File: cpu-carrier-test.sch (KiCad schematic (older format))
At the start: 10 parts, among them SW1 SW_Push

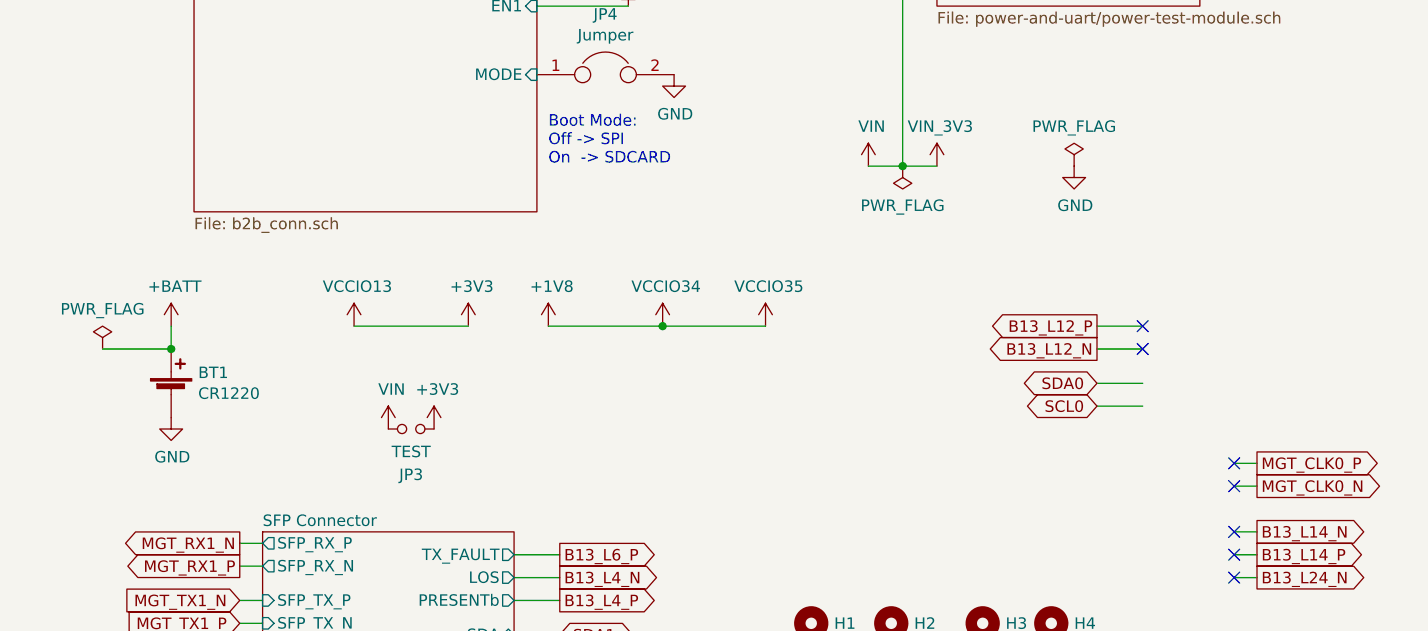
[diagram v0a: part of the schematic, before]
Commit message: connected lan9254 power to board power
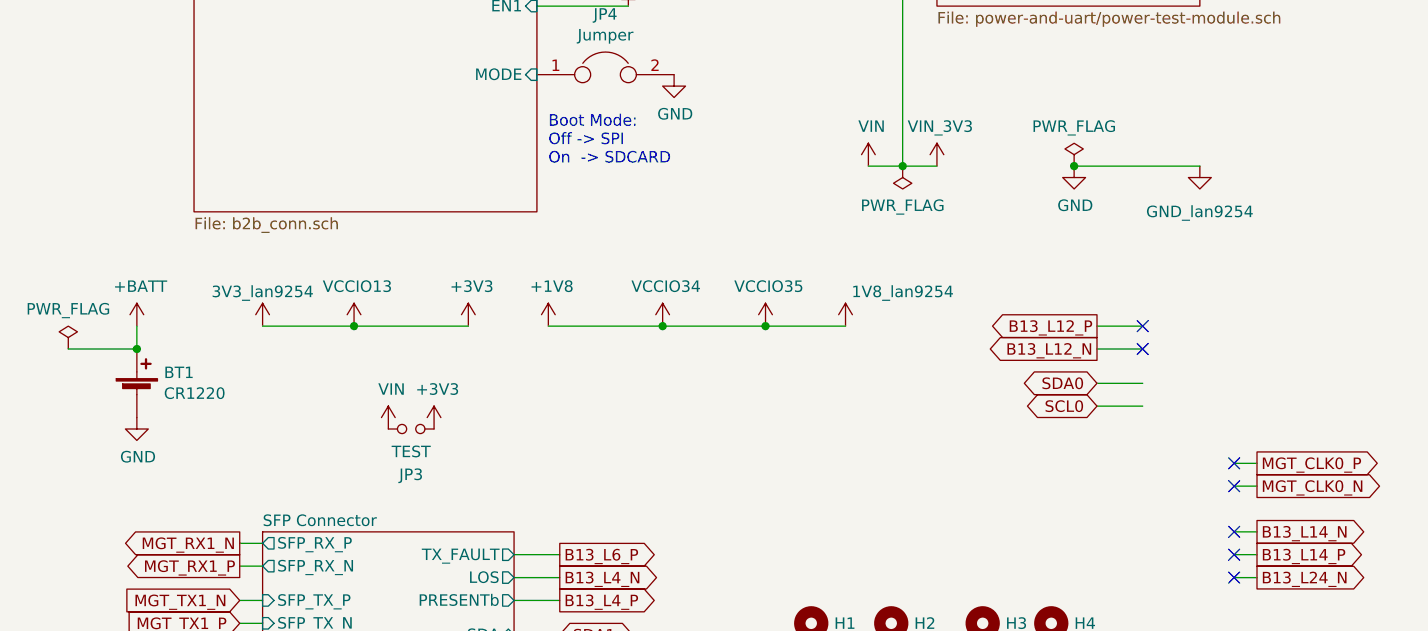
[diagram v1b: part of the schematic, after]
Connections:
- wire segments 84 -> 87
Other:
- moved on the sheet: BT1
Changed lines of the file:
@@
 L Device:Battery_Cell BT?
 U 1 1 5C5255D6
-P 1250 3550
+P 1100 3550
 AR Path="/5CEAC2F1/5C5255D6" Ref="BT?"  Part="1"
 AR Path="/5C5255D6" Ref="BT1"  Part="1"
-F 0 "BT1" H 1368 3646 50  0000 L CNN
-F 1 "CR1220" H 1368 3555 50  0000 L CNN
-F 2 "Battery:BatteryHolder_Keystone_500" V 1250 3610 50  0001 C CNN
-F 3 "~" V 1250 3610 50  0001 C CNN
-F 4 "Keystone" H 1250 3550 50  0001 C CNN "Manufacturer"
-F 5 "500" H 1250 3550 50  0001 C CNN "Part"
-	1    1250 3550
+F 0 "BT1" H 1218 3646 50  0000 L CNN
+F 1 "CR1220" H 1218 3555 50  0000 L CNN
+F 2 "Battery:BatteryHolder_Keystone_500" V 1100 3610 50  0001 C CNN
+F 3 "~" V 1100 3610 50  0001 C CNN
+F 4 "Keystone" H 1100 3550 50  0001 C CNN "Manufacturer"
+F 5 "500" H 1100 3550 50  0001 C CNN "Part"
+	1    1100 3550
 	1    0    0    -1
 $EndComp
@@
 L power:GND #PWR?
 U 1 1 5C5255DD
-P 1250 3650
+P 1100 3650
 AR Path="/5CEAC2F1/5C5255DD" Ref="#PWR?"  Part="1"
 AR Path="/5C5255DD" Ref="#PWR?"  Part="1"
-F 0 "#PWR?" H 1250 3400 50  0001 C CNN
-F 1 "GND" H 1255 3477 50  0000 C CNN
-F 2 "" H 1250 3650 50  0001 C CNN
-F 3 "" H 1250 3650 50  0001 C CNN
-	1    1250 3650
+F 0 "#PWR?" H 1100 3400 50  0001 C CNN
+F 1 "GND" H 1105 3477 50  0000 C CNN
+F 2 "" H 1100 3650 50  0001 C CNN
+F 3 "" H 1100 3650 50  0001 C CNN
+	1    1100 3650
 	1    0    0    -1
 $EndComp
@@
 L power:PWR_FLAG #FLG?
 U 1 1 5C5255E3
-P 950 3350
+P 800 3350
 AR Path="/5CEAC2F1/5C5255E3" Ref="#FLG?"  Part="1"
 AR Path="/5C5255E3" Ref="#FLG?"  Part="1"
-F 0 "#FLG?" H 950 3425 50  0001 C CNN
-F 1 "PWR_FLAG" H 950 3524 50  0000 C CNN
-F 2 "" H 950 3350 50  0001 C CNN
-F 3 "~" H 950 3350 50  0001 C CNN
-	1    950  3350
-	1    0    0    -1
-$EndComp
-Wire Wire Line
-	950  3350 1250 3350
+F 0 "#FLG?" H 800 3425 50  0001 C CNN
+F 1 "PWR_FLAG" H 800 3524 50  0000 C CNN
+F 2 "" H 800 3350 50  0001 C CNN
+F 3 "~" H 800 3350 50  0001 C CNN
+	1    800  3350
+	1    0    0    -1
+$EndComp
+Wire Wire Line
+	800  3350 1100 3350
 $Comp
 L power:+BATT #PWR?
 U 1 1 5C5255EA
-P 1250 3250
+P 1100 3250
 AR Path="/5CEAC2F1/5C5255EA" Ref="#PWR?"  Part="1"
 AR Path="/5C5255EA" Ref="#PWR?"  Part="1"
-F 0 "#PWR?" H 1250 3100 50  0001 C CNN
-F 1 "+BATT" H 1265 3423 50  0000 C CNN
-F 2 "" H 1250 3250 50  0001 C CNN
-F 3 "" H 1250 3250 50  0001 C CNN
-	1    1250 3250
-	1    0    0    -1
-$EndComp
-Wire Wire Line
-	1250 3250 1250 3350
-Connection ~ 1250 3350
+F 0 "#PWR?" H 1100 3100 50  0001 C CNN
+F 1 "+BATT" H 1115 3423 50  0000 C CNN
+F 2 "" H 1100 3250 50  0001 C CNN
+F 3 "" H 1100 3250 50  0001 C CNN
+	1    1100 3250
+	1    0    0    -1
+$EndComp
+Wire Wire Line
+	1100 3250 1100 3350
+Connection ~ 1100 3350
 $Comp
 L trigbox:VCCIO13 #PWR?
@@
 F52 "FPGA_IO1_DIR" I L 8300 6400 50
 $EndSheet
+$Comp
+L lan9254_project:+1V8 #PWR?
+U 1 1 60E7C109
+P 4200 3250
+AR Path="/60DC28BD/60E7C109" Ref="#PWR?"  Part="1"
+AR Path="/60E7C109" Ref="#PWR?"  Part="1"
+AR Path="/60DB2574/60E7C109" Ref="#PWR?"  Part="1"
+AR Path="/60E70F2C/60E7C109" Ref="#PWR?"  Part="1"
+F 0 "#PWR?" H 4200 3100 50  0001 C CNN
+F 1 "+1V8" H 4215 3423 50  0001 C CNN
+F 2 "" H 4200 3250 50  0001 C CNN
+F 3 "" H 4200 3250 50  0001 C CNN
+F 4 "1V8_lan9254" H 4450 3400 50  0000 C CNN "Field4"
+	1    4200 3250
+	1    0    0    -1
+$EndComp
+Wire Wire Line
+	4200 3250 3850 3250
+Connection ~ 3850 3250
+$Comp
+L lan9254_project:+3V3 #PWR?
+U 1 1 60E83E35
+P 1650 3250
+AR Path="/60DC28BD/60E83E35" Ref="#PWR?"  Part="1"
+AR Path="/60E83E35" Ref="#PWR?"  Part="1"
+AR Path="/60DB2574/60E83E35" Ref="#PWR?"  Part="1"
+AR Path="/60E70F2C/60E83E35" Ref="#PWR?"  Part="1"
+F 0 "#PWR?" H 1650 3100 50  0001 C CNN
+F 1 "+3V3" H 1665 3423 50  0001 C CNN
+F 2 "" H 1650 3250 50  0001 C CNN
+F 3 "" H 1650 3250 50  0001 C CNN
+F 4 "3V3_lan9254" H 1650 3400 50  0000 C CNN "Field4"
+	1    1650 3250
+	1    0    0    -1
+$EndComp
+Wire Wire Line
+	1650 3250 2050 3250
+Connection ~ 2050 3250
+$Comp
+L lan9254_project:GND #PWR?
+U 1 1 60E8D23A
+P 5750 2550
+AR Path="/60DC28BD/60E8D23A" Ref="#PWR?"  Part="1"
+AR Path="/60E8D23A" Ref="#PWR?"  Part="1"
+AR Path="/60DB2574/60E8D23A" Ref="#PWR?"  Part="1"
+AR Path="/60E70F2C/60E8D23A" Ref="#PWR?"  Part="1"
+F 0 "#PWR?" H 5750 2300 50  0001 C CNN
+F 1 "GND" H 5755 2377 50  0001 C CNN
+F 2 "" H 5750 2550 50  0001 C CNN
+F 3 "" H 5750 2550 50  0001 C CNN
+F 4 "GND_lan9254" H 5750 2350 50  0000 C CNN "Field4"
+	1    5750 2550
+	1    0    0    -1
+$EndComp
+Wire Wire Line
+	5750 2550 5200 2550
+Connection ~ 5200 2550
 $EndSCHEMATC

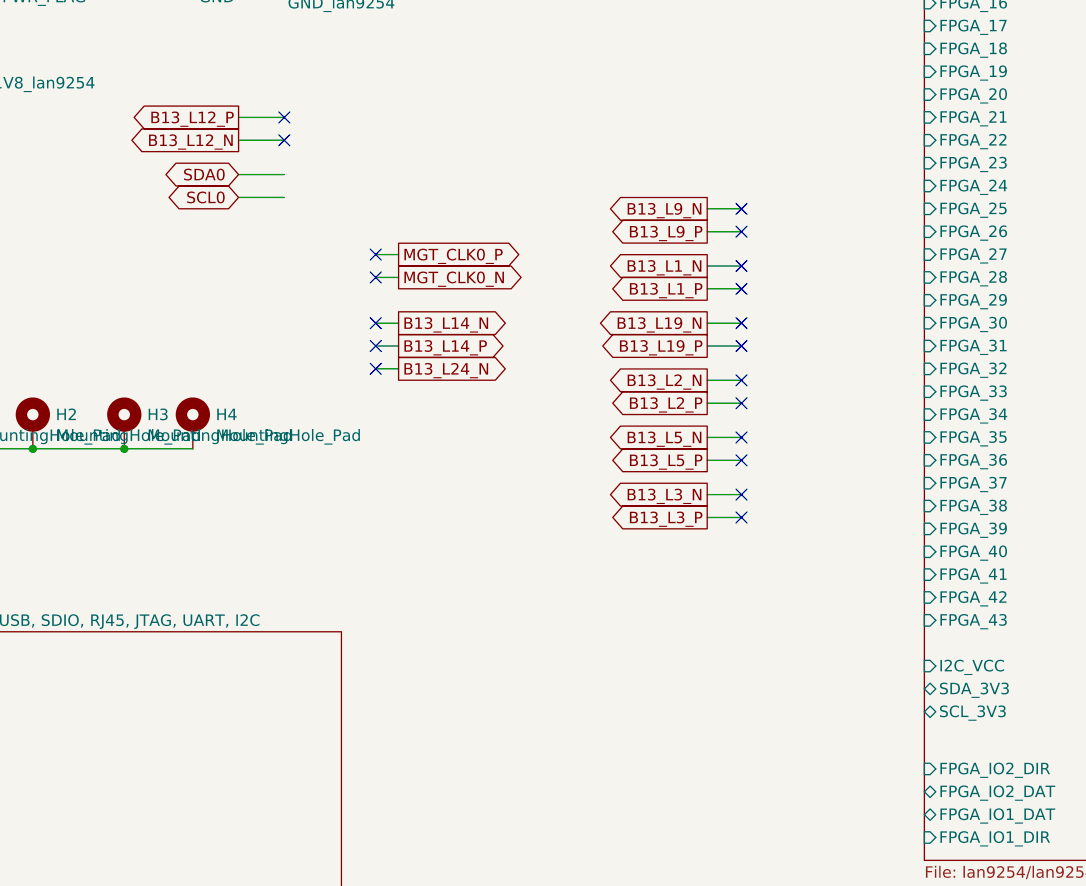
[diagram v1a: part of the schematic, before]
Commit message: connected lan9254 i2c to baseboard SDA0/SDC0
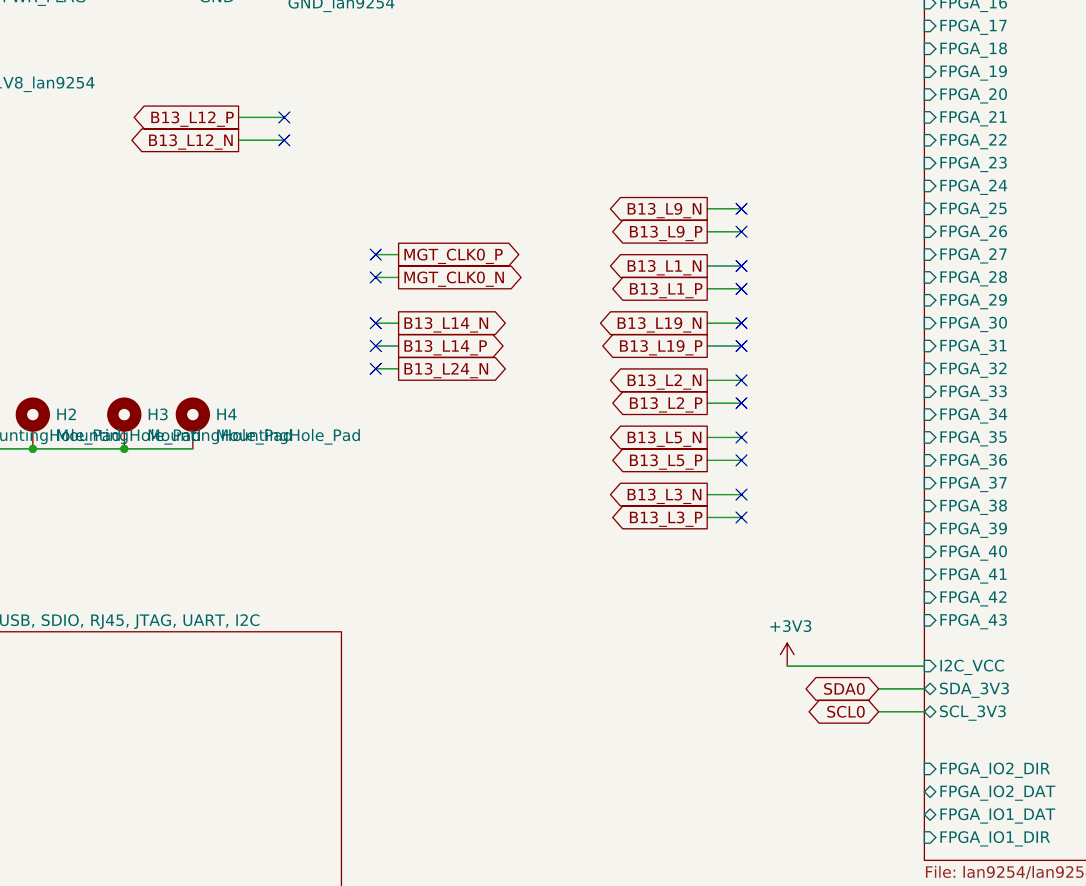
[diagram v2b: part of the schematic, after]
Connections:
- wire segments 87 -> 88
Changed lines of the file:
@@
 $EndSheet
 Wire Wire Line
-	5300 3500 5500 3500
-Wire Wire Line
-	5300 3600 5500 3600
+	8100 5750 8300 5750
+Wire Wire Line
+	8100 5850 8300 5850
 $Sheet
 S 1650 4150 1100 650
@@
 Text GLabel 2950 4700 2    50   BiDi ~ 0
 SCL1
-Text GLabel 5300 3500 0    50   BiDi ~ 0
+Text GLabel 8100 5750 0    50   BiDi ~ 0
 SDA0
-Text GLabel 5300 3600 0    50   BiDi ~ 0
+Text GLabel 8100 5850 0    50   BiDi ~ 0
 SCL0
 $Comp
@@
 	5750 2550 5200 2550
 Connection ~ 5200 2550
+$Comp
+L power:+3V3 #PWR?
+U 1 1 60E53427
+P 7700 5650
+AR Path="/5BE73D36/60E53427" Ref="#PWR?"  Part="1"
+AR Path="/5CEAC2F1/60E53427" Ref="#PWR?"  Part="1"
+AR Path="/60E53427" Ref="#PWR?"  Part="1"
+F 0 "#PWR?" H 7700 5500 50  0001 C CNN
+F 1 "+3V3" H 7715 5823 50  0000 C CNN
+F 2 "" H 7700 5650 50  0001 C CNN
+F 3 "" H 7700 5650 50  0001 C CNN
+	1    7700 5650
+	1    0    0    -1
+$EndComp
+Wire Wire Line
+	7700 5650 8300 5650
 $EndSCHEMATC

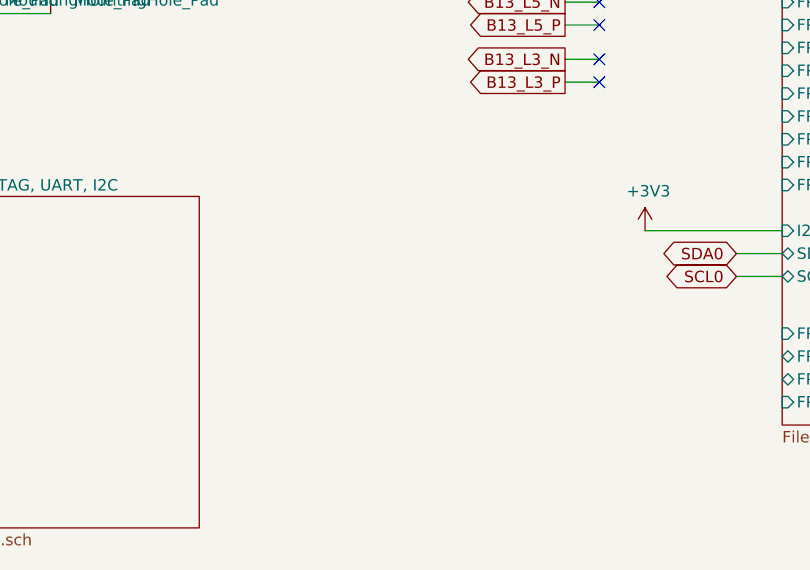
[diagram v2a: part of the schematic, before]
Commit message: converted local- to global labels for B34/B34 B2B pins
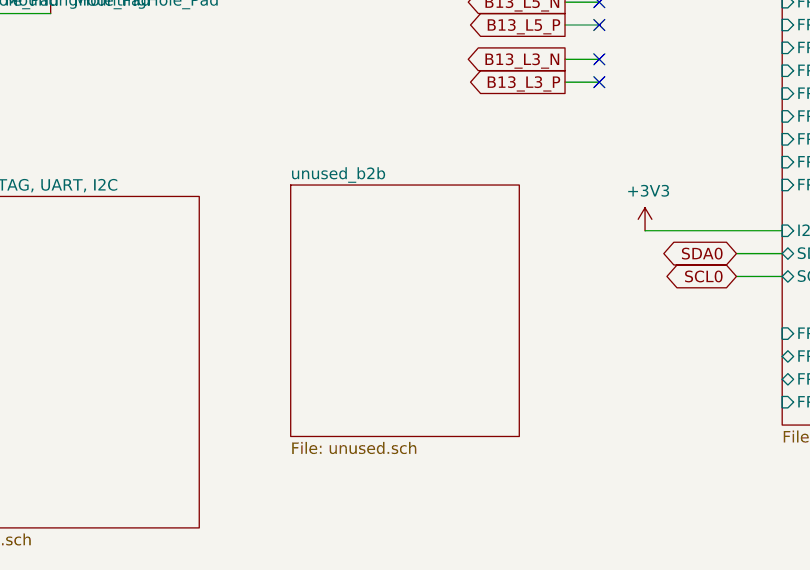
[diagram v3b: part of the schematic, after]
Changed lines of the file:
@@
 $Descr USLetter 11000 8500
 encoding utf-8
-Sheet 1 11
+Sheet 1 12
 Title ""
 Date ""
@@
 Wire Wire Line
 	7700 5650 8300 5650
+$Sheet
+S 6150 5450 1000 1100
+U 60F0717C
+F0 "unused_b2b" 50
+F1 "unused.sch" 50
+$EndSheet
 $EndSCHEMATC

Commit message: cont. work; all connections done now
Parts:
- added D1, D2, D3, D4, D5, D6, D7, D8: LED, LED_SMD:LED_0603_1608Metric, symbol Device:LED
- added R10, R3, R4, R5, R6, R7, R8, R9: 1k, Resistor_SMD:R_0603_1608Metric, symbol Device:R_Small
- R1: renamed from R19; value R10k -> 10k
- R2: renamed from R20; value R10k -> 10k
- renumbered JP3 to JP1, JP4 to JP2
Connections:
- net labels added: B13_L18_N, B13_L18_P, B13_L21_N, B13_L21_P, B34_L12_P, B34_L15_N, B34_L15_P, B34_L18_N, B34_L2_N, B34_L2_P, B34_L6_N, B34_L6_P, B34_L7_N, B34_L8_P, B35_L0, B35_L10_N, B35_L10_P, B35_L11_N, B35_L12_N, B35_L12_P, B35_L13_N, B35_L13_P, B35_L14_N, B35_L14_P, B35_L15_N, B35_L15_P, B35_L16_N, B35_L16_P, B35_L17_N, B35_L17_P, B35_L18_N, B35_L18_P, B35_L20_N, B35_L20_P, B35_L21_P, B35_L22_N, B35_L22_P, B35_L23_N, B35_L23_P, B35_L24_N, B35_L24_P, B35_L25, B35_L2_N, B35_L2_P, B35_L3_N, B35_L4_P, B35_L5_N, B35_L6_N, B35_L7_N, B35_L8_P, B35_L9_N, B35_L9_P
- net labels removed: B13_L11_N, B13_L11_P, B13_L12_N, B13_L12_P, B13_L13_N, B13_L13_P, B13_L14_N, B13_L14_P, B13_L16_N, B13_L16_P, B13_L17_N, B13_L17_P, B13_L19_N, B13_L19_P, B13_L1_N, B13_L1_P, B13_L24_N, B13_L2_N, B13_L2_P, B13_L3_N, B13_L3_P, B13_L5_N, B13_L5_P, B13_L9_N, B13_L9_P, MGT_CLK0_N, MGT_CLK0_P
- wire segments 88 -> 121
- no-connect marks 47 -> 16
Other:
- note added: "GREEN LED"
- note added: "Mounting Holes"
- note added: "RED LED"
- moved on the sheet: H1, H2, H3, H4

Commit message: added more component values/part numbers
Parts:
- D1, D2, D3, D4: Part 150060GS75000 -> 150060GS75000
- D5, D6, D7: Part 150060RS75000 -> 150060RS75000
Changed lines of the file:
@@
 F 3 "~" H 5250 3500 50  0001 C CNN
 F 4 "Wurth" H 5250 3500 50  0001 C CNN "Manufacturer"
-F 5 " 150060GS75000 " H 5250 3500 50  0001 C CNN "Part"
+F 5 "150060GS75000" H 5250 3500 50  0001 C CNN "Part"
 	1    5250 3500
 	-1   0    0    1
@@
 F 3 "~" H 5250 3850 50  0001 C CNN
 F 4 "Wurth" H 5250 3850 50  0001 C CNN "Manufacturer"
-F 5 " 150060GS75000 " H 5250 3850 50  0001 C CNN "Part"
+F 5 "150060GS75000" H 5250 3850 50  0001 C CNN "Part"
 	1    5250 3850
 	-1   0    0    1
@@
 F 3 "~" H 5250 4200 50  0001 C CNN
 F 4 "Wurth" H 5250 4200 50  0001 C CNN "Manufacturer"
-F 5 " 150060GS75000 " H 5250 4200 50  0001 C CNN "Part"
+F 5 "150060GS75000" H 5250 4200 50  0001 C CNN "Part"
 	1    5250 4200
 	-1   0    0    1
@@
 F 3 "~" H 5250 4550 50  0001 C CNN
 F 4 "Wurth" H 5250 4550 50  0001 C CNN "Manufacturer"
-F 5 " 150060GS75000 " H 5250 4550 50  0001 C CNN "Part"
+F 5 "150060GS75000" H 5250 4550 50  0001 C CNN "Part"
 	1    5250 4550
 	-1   0    0    1
@@
 F 3 "~" H 5250 5000 50  0001 C CNN
 F 4 "Wurth" H 5250 5000 50  0001 C CNN "Manufacturer"
-F 5 " 150060RS75000 " H 5250 5000 50  0001 C CNN "Part"
+F 5 "150060RS75000" H 5250 5000 50  0001 C CNN "Part"
 	1    5250 5000
 	-1   0    0    1
@@
 F 3 "~" H 5250 5350 50  0001 C CNN
 F 4 "Wurth" H 5250 5350 50  0001 C CNN "Manufacturer"
-F 5 " 150060RS75000 " H 5250 5350 50  0001 C CNN "Part"
+F 5 "150060RS75000" H 5250 5350 50  0001 C CNN "Part"
 	1    5250 5350
 	-1   0    0    1
@@
 F 3 "~" H 5250 5750 50  0001 C CNN
 F 4 "Wurth" H 5250 5750 50  0001 C CNN "Manufacturer"
-F 5 " 150060RS75000 " H 5250 5750 50  0001 C CNN "Part"
+F 5 "150060RS75000" H 5250 5750 50  0001 C CNN "Part"
 	1    5250 5750
 	-1   0    0    1
